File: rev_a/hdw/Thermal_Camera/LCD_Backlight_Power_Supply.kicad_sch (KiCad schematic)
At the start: 0 parts

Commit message: added battery circuitry, LCD backlight
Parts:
- added C?: 10uF, Capacitors_SMD:C_1206, symbol Custom_Library:C_Custom
- added C? (x2): 0.1uF, Capacitors_SMD:C_0603, symbol Custom_Library:C_Custom
- added C?: 1uF, Capacitors_SMD:C_0603, symbol Custom_Library:C_Custom
- added L?: 22uH, symbol Custom_Library:L_Custom
- added R?: R, Resistors_SMD:R_0603, symbol Custom_Library:R_Custom
- added R?: 0.02, Resistors_SMD:R_0612, symbol Custom_Library:R_Custom
- added R? (x2): 10, Resistors_SMD:R_0603, symbol Custom_Library:R_Custom
- added U?: LT3465, Package_TO_SOT_SMD:TSOT-23-6, symbol Driver_LED:LT3465
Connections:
- new net: L?.1, U?.6 (SW)
- new net: C?.1, C?.1, R?.1, R?.2, U?.1 (VOUT)
- new net BACKLIGHT_ANODE: R?.2, R?.2
- new net BACKLIGHT_CATHODE: R?.1, U?.3 (FB)
- new net GND: C?.2, C?.2, C?.2, C?.2, R?.2, U?.2 (GND)
- new net VCOM: C?.1, C?.1, L?.2, U?.5 (VIN)
- new net VLED_SNS+: R?.1
- new net VLED_SNS-: R?.1
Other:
- note added: "Add PWM filter"

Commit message: added PIC32 bypass, SD card load switch, other random junk
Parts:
- added C?: 0.1uF, Capacitors_SMD:C_0603, symbol Custom_Library:C_Custom
- added R1501 (x2): 10k, Resistors_SMD:R_0603, symbol Custom_Library:R_Custom
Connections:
- net GND: now also C?.2
- net at U?.4 (CTRL): now also C?.1, R1501.2, R1501.2
- new net BACKLIGHT_PWM: R1501.1, R1501.1
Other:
- note removed: "Add PWM filter"

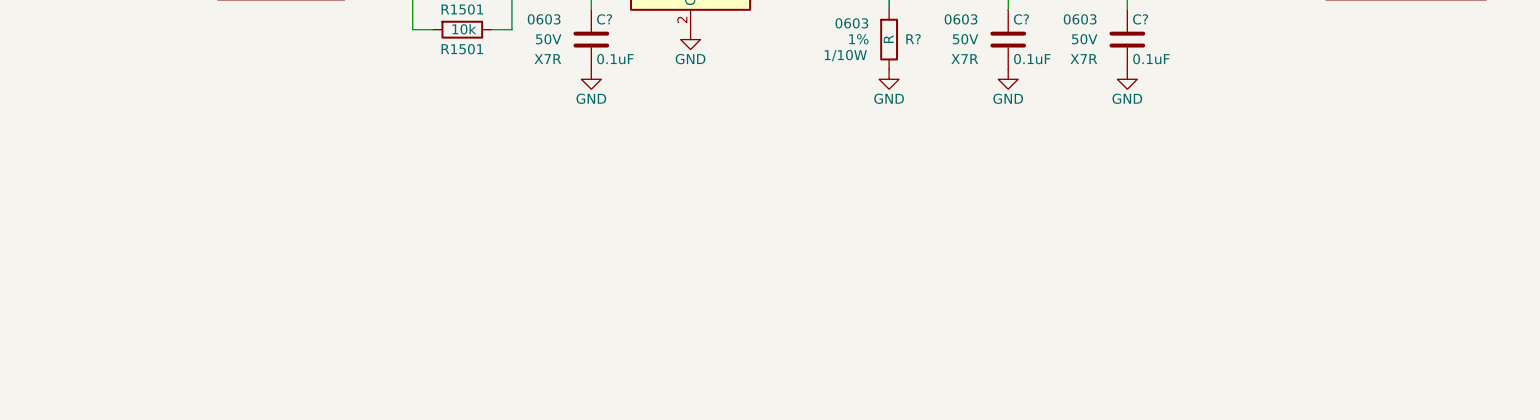
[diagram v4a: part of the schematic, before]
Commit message: added some LCD components
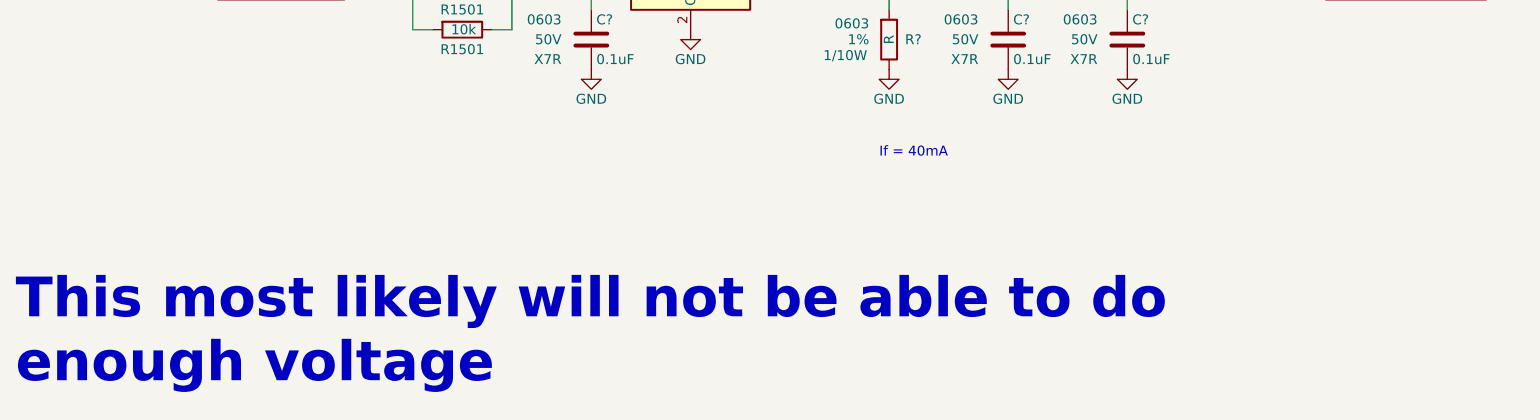
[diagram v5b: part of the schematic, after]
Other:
- note added: "If = 40mA"
- note added: "This most likely will not be able to do enough voltage"
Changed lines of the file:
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@@
     (stroke (width 0) (type default))
+  )
+  (text "If = 40mA" (at 140.97 106.68 0)
+    (effects (font (size 1.27 1.27)) (justify left bottom))
+  )
+  (text "This most likely will not be able to do\nenough voltage"
+    (at 30.48 135.89 0)
+    (effects (font (face "Courier New") (size 5.08 5.08) (thickness 1.016) bold (color 194 0 0 1)) (justify left bottom))
   )
   (global_label "BACKLIGHT_ANODE" (shape passive) (at 198.12 80.01 0) (fields_autoplaced)

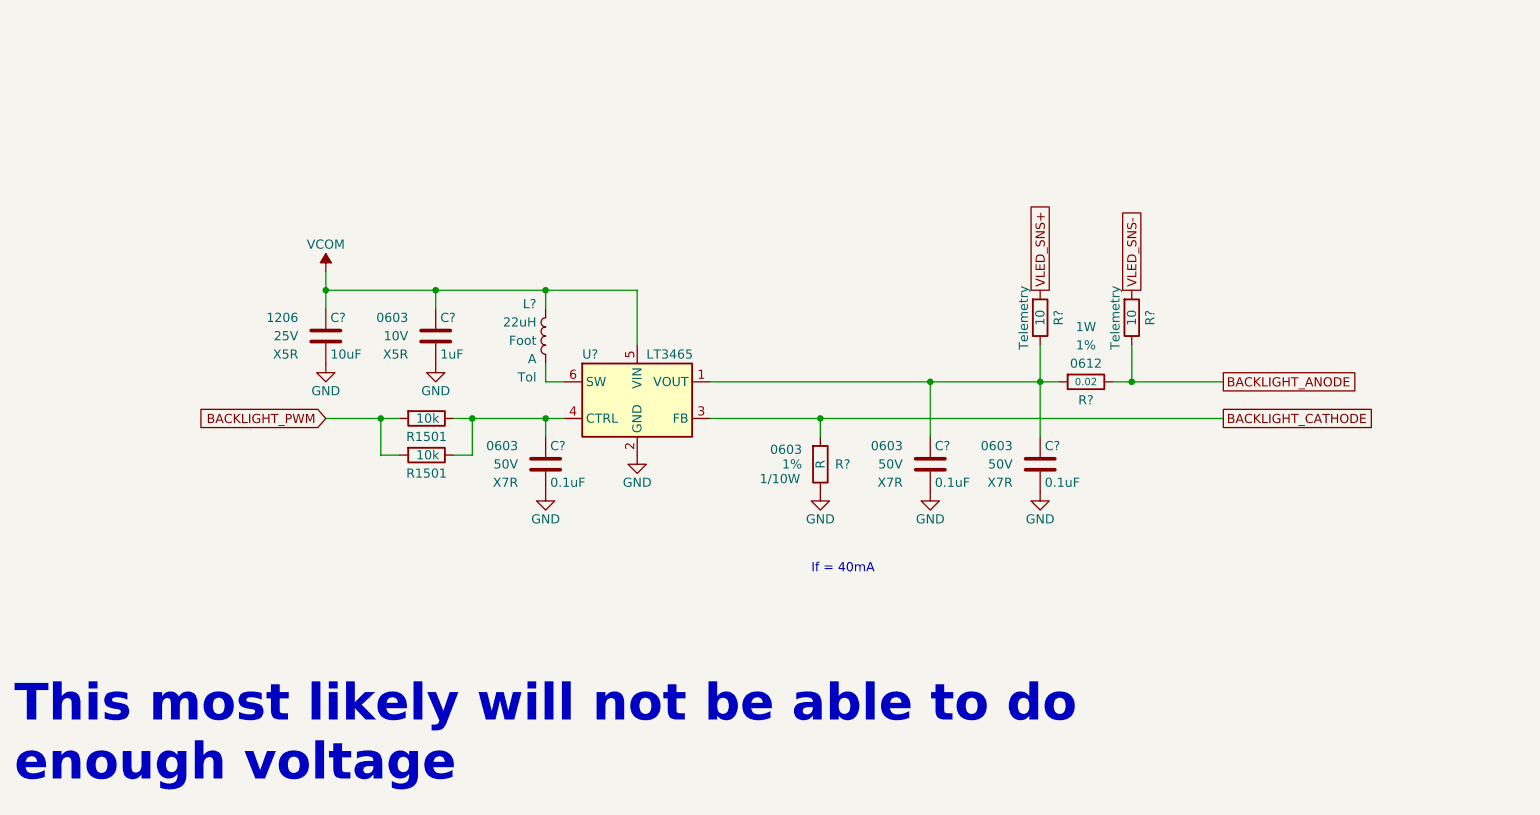
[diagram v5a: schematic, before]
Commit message: added pull resistors for LCD signals
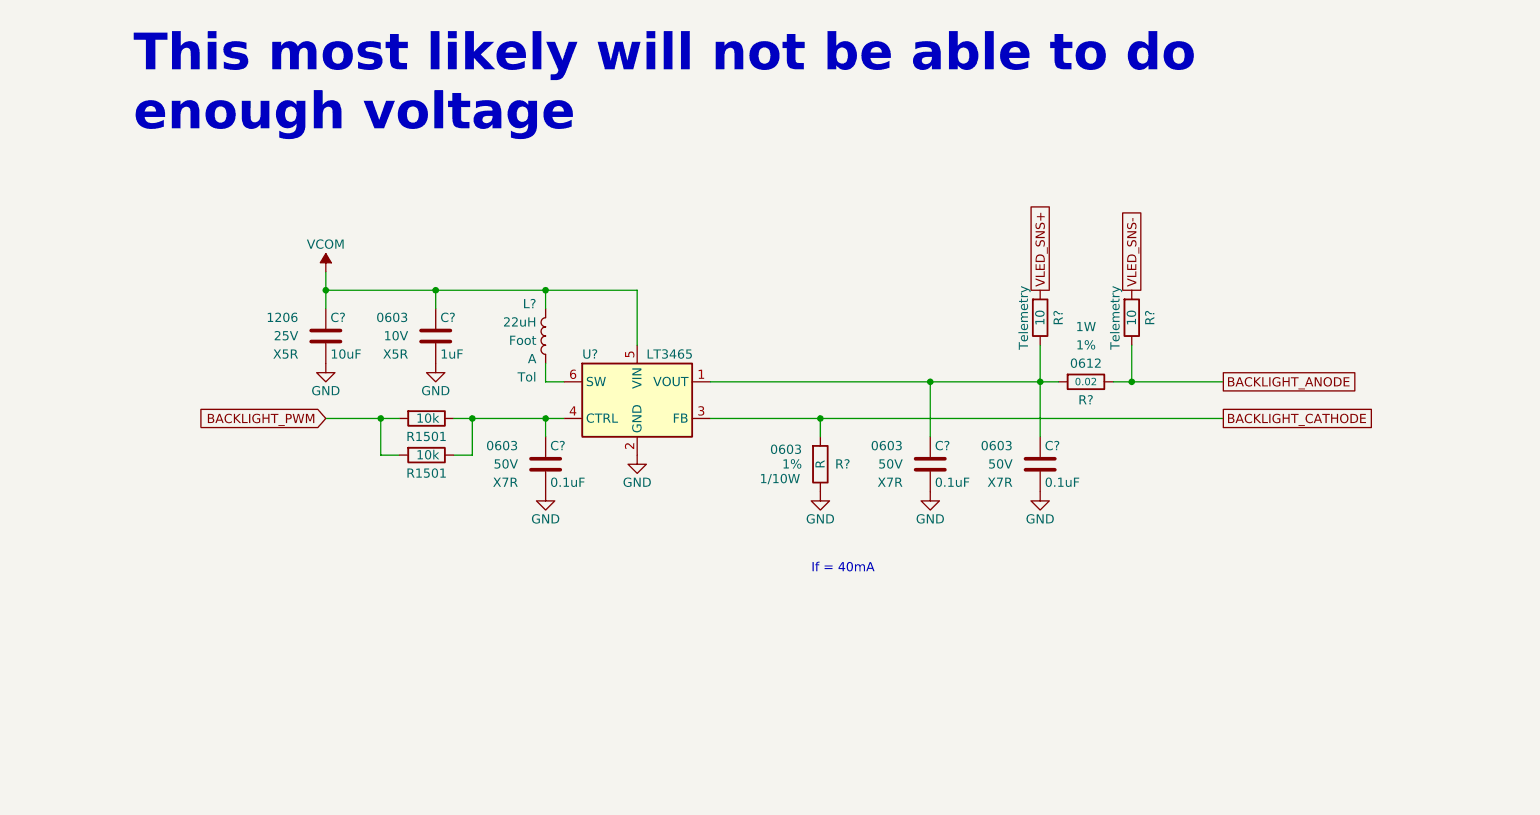
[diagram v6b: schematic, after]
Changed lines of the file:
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@@
   )
   (text "This most likely will not be able to do\nenough voltage"
-    (at 30.48 135.89 0)
+    (at 46.99 45.72 0)
     (effects (font (face "Courier New") (size 5.08 5.08) (thickness 1.016) bold (color 194 0 0 1)) (justify left bottom))
   )

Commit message: changed LED backlight driver
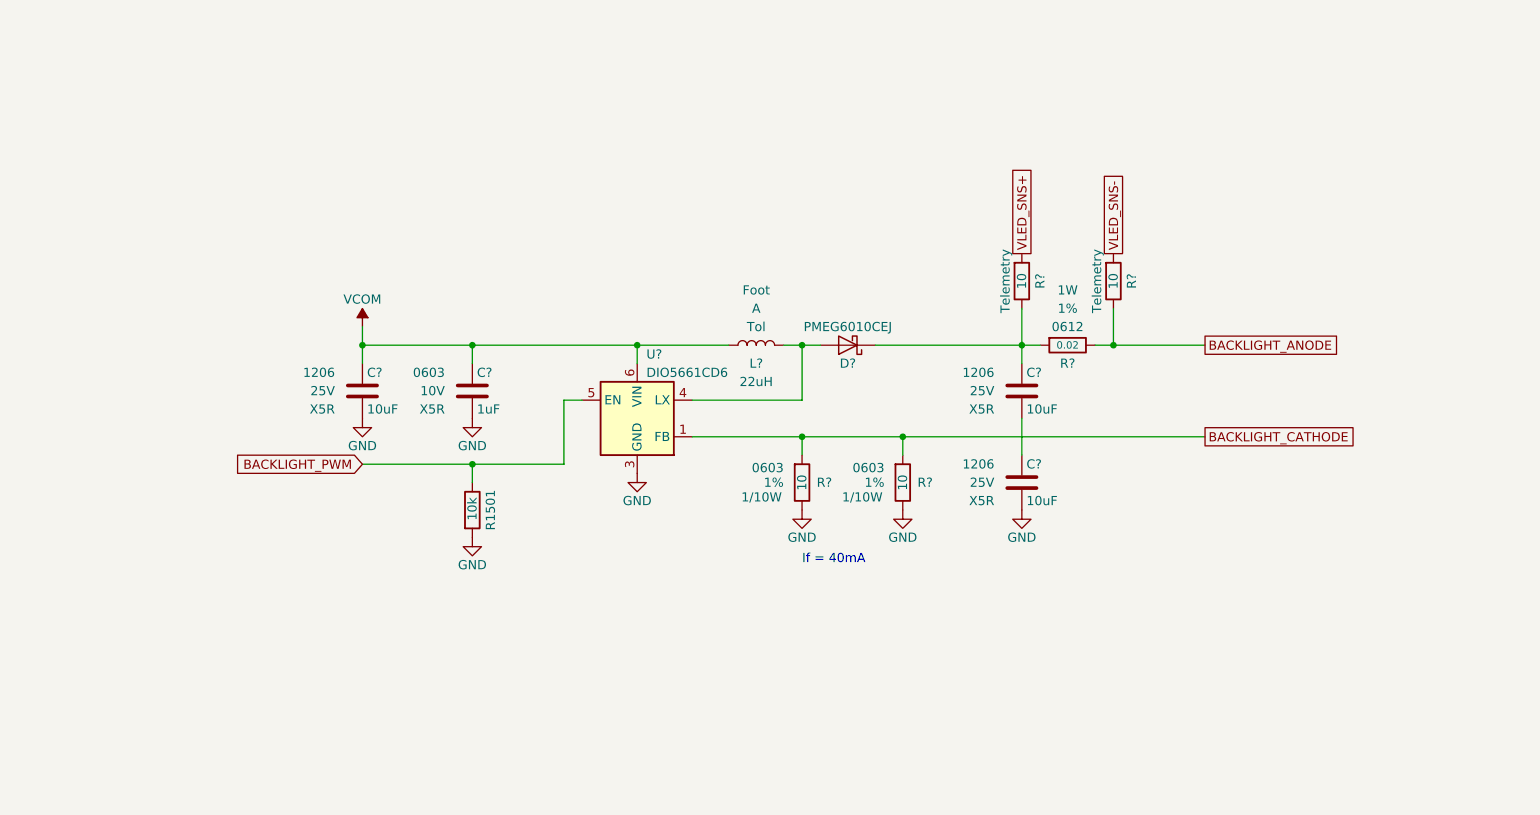
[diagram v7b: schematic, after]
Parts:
- removed C?: 10uF, Capacitors_SMD:C_1206, symbol Custom_Library:C_Custom
- removed C? (x3): 0.1uF, Capacitors_SMD:C_0603, symbol Custom_Library:C_Custom
- removed C?: 1uF, Capacitors_SMD:C_0603, symbol Custom_Library:C_Custom
- removed R1501 (x2): 10k, Resistors_SMD:R_0603, symbol Custom_Library:R_Custom
- removed R?: R, Resistors_SMD:R_0603, symbol Custom_Library:R_Custom
- removed R?: 0.02, Resistors_SMD:R_0612, symbol Custom_Library:R_Custom
- removed R? (x2): 10, Resistors_SMD:R_0603, symbol Custom_Library:R_Custom
- removed U?: LT3465, Package_TO_SOT_SMD:TSOT-23-6, symbol Driver_LED:LT3465
- added C? (x3): 10uF, Capacitors_SMD:C_1206, symbol Custom_Library:C_Custom
- added C?: 1uF, Capacitors_SMD:C_0603, symbol Custom_Library:C_Custom
- added D?: PMEG6010CEJ, Diode_SMD:D_SOD-323F, symbol Diode:PMEG6010CEJ
- added R1501: 10k, Resistors_SMD:R_0603, symbol Custom_Library:R_Custom
- added R? (x4): 10, Resistors_SMD:R_0603, symbol Custom_Library:R_Custom
- added R?: 0.02, Resistors_SMD:R_0612, symbol Custom_Library:R_Custom
- added U?: DIO5661CD6, Package_DFN_QFN:DFN-6-1EP_2x2mm_P0.65mm_EP1x1.6mm, symbol Driver_LED:DIO5661CD6
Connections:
- net BACKLIGHT_ANODE: now also R?.2, R?.2
- net BACKLIGHT_CATHODE: now also R?.1, R?.1, U?.1 (FB)
- net BACKLIGHT_PWM: now also R1501.2, U?.5 (EN)
- net GND: now also C?.2, C?.2, C?.2, R1501.1, R?.2, R?.2, U?.3 (GND), U?.7 (GND)
- net VCOM: now also L?.1, C?.1, C?.1, U?.6 (VIN); no longer L?.2
- net VLED_SNS+: now also R?.1
- net VLED_SNS-: now also R?.1
- new net: C?.1, D?.1 (K), R?.1, R?.2
- new net: D?.2 (A), L?.2, U?.4 (LX)
- new net: C?.1, C?.2
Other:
- note removed: "This most likely will not be able to do enough voltage"
- moved on the sheet: L?

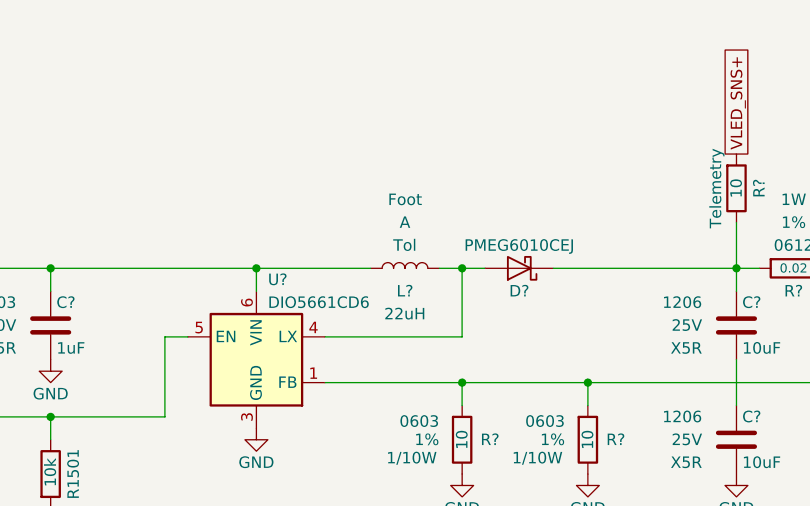
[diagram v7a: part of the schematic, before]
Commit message: chose backlight boost inductor
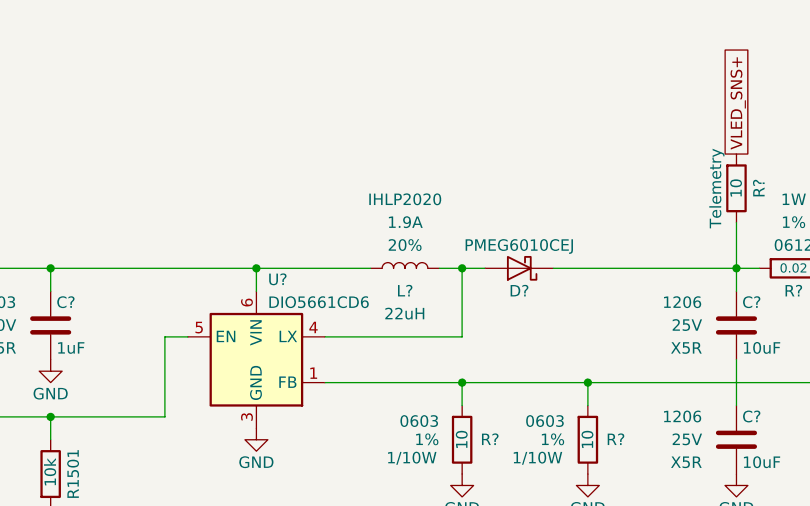
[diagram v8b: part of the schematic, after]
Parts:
- L?: footprint (none) -> Inductor_SMD:L_Vishay_IHLP-2020; Ampacity A -> 1.9A; Digi-Key PN (none) -> 541-1243-1-ND; Tolerance Tol -> 20%; display_footprint Foot -> IHLP2020
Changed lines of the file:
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@@
   (title_block
     (title "Thermal Camera")
-    (date "2023-11-13")
+    (date "2023-12-07")
     (rev "PRELIM")
     (company "Drew Maatman and Michael Laffin")
@@
       (effects (font (size 1.27 1.27)))
     )
-    (property "Footprint" "" (at 133.35 74.93 0)
+    (property "Footprint" "Inductor_SMD:L_Vishay_IHLP-2020" (at 133.35 74.93 0)
       (effects (font (size 1.27 1.27)) hide)
     )
@@
       (effects (font (size 1.27 1.27)) hide)
     )
-    (property "display_footprint" "Foot" (at 133.35 67.31 90)
-      (effects (font (size 1.27 1.27)))
-    )
-    (property "Ampacity" "A" (at 133.35 69.85 90)
-      (effects (font (size 1.27 1.27)))
-    )
-    (property "Tolerance" "Tol" (at 133.35 72.39 90)
-      (effects (font (size 1.27 1.27)))
-    )
-    (property "Digi-Key PN" "" (at 133.35 74.93 0)
-      (effects (font (size 1.27 1.27)) hide)
-    )
+    (property "display_footprint" "IHLP2020" (at 133.35 67.31 90)
+      (effects (font (size 1.27 1.27)))
+    )
+    (property "Ampacity" "1.9A" (at 133.35 69.85 90)
+      (effects (font (size 1.27 1.27)))
+    )
+    (property "Tolerance" "20%" (at 133.35 72.39 90)
+      (effects (font (size 1.27 1.27)))
+    )
+    (property "Digi-Key PN" "541-1243-1-ND" (at 133.35 74.93 0)
+      (effects (font (size 1.27 1.27)) hide)
+    )
